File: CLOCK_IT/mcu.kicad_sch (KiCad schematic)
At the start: 25 parts, among them IC1 APS6404L-3SQR-SN, U1 ESP32-S3R8, U2 W25Q128JVSIQ

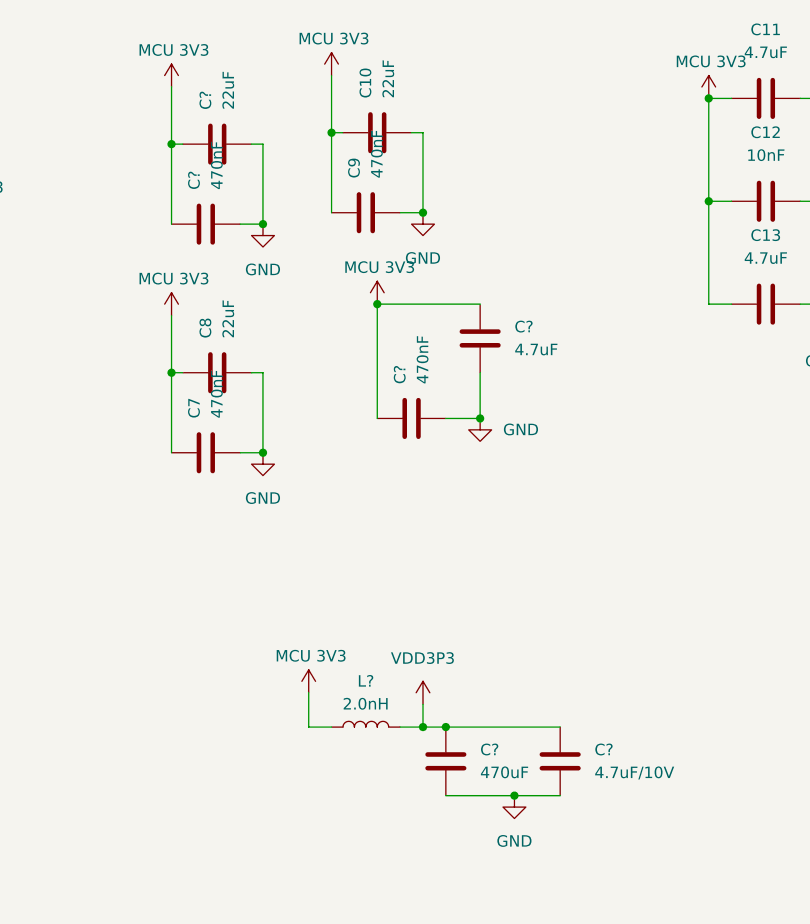
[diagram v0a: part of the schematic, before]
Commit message: :style: renaming capaciors, checking for errors
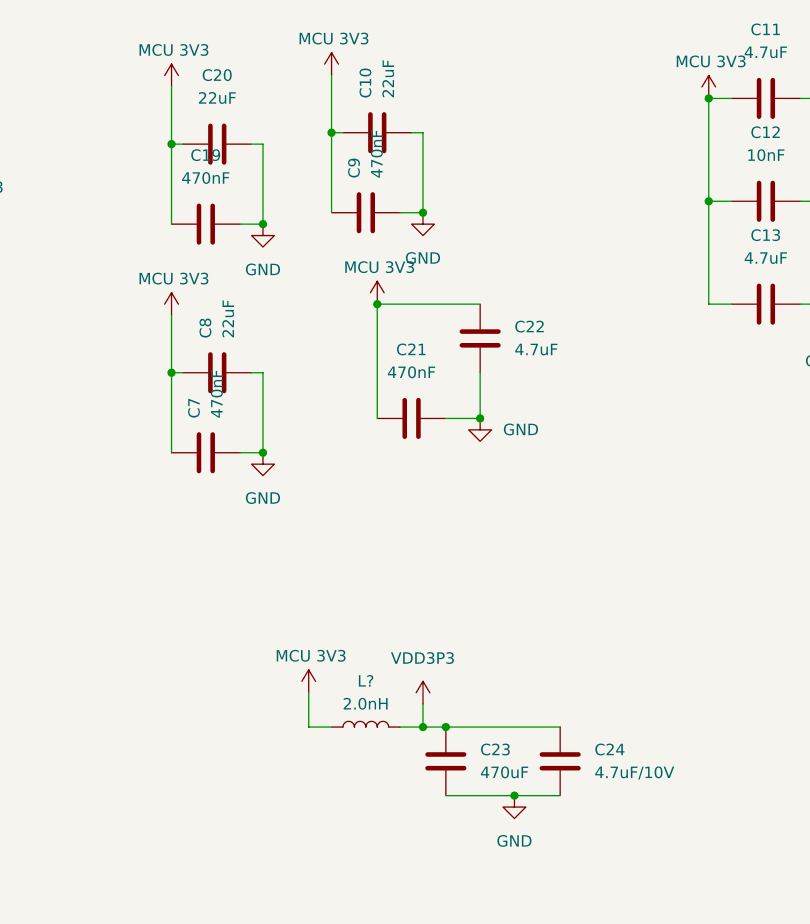
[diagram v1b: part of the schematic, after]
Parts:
- gave numbers to parts that had none: 6
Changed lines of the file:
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@@
 		(dnp no)
 		(fields_autoplaced yes)
-		(property "Reference" "C?"
+		(property "Reference" "C23"
 			(at 233.68 93.9799 0)
 			(effects
@@
 			(project "CLOCK_IT"
 				(path "/6c8f4e2a-0be1-4eb1-92e1-07339040f4c9/25a0942f-4692-4437-8e26-71d966c353a5"
-					(reference "C?")
+					(reference "C23")
 					(unit 1)
 				)
@@
 		(dnp no)
 		(fields_autoplaced yes)
-		(property "Reference" "C?"
-			(at 224.7899 53.34 0)
-			(effects
-				(font
-					(size 1.27 1.27)
-				)
-				(justify left)
+		(property "Reference" "C21"
+			(at 226.06 49.53 90)
+			(effects
+				(font
+					(size 1.27 1.27)
+				)
 			)
 		)
 		(property "Value" "470nF"
-			(at 227.3299 53.34 0)
-			(effects
-				(font
-					(size 1.27 1.27)
-				)
-				(justify left)
+			(at 226.06 52.07 90)
+			(effects
+				(font
+					(size 1.27 1.27)
+				)
 			)
 		)
@@
 			(project "CLOCK_IT"
 				(path "/6c8f4e2a-0be1-4eb1-92e1-07339040f4c9/25a0942f-4692-4437-8e26-71d966c353a5"
-					(reference "C?")
+					(reference "C21")
 					(unit 1)
 				)
@@
 		(dnp no)
 		(fields_autoplaced yes)
-		(property "Reference" "C?"
-			(at 201.9299 31.75 0)
-			(effects
-				(font
-					(size 1.27 1.27)
-				)
-				(justify left)
+		(property "Reference" "C19"
+			(at 203.2 27.94 90)
+			(effects
+				(font
+					(size 1.27 1.27)
+				)
 			)
 		)
 		(property "Value" "470nF"
-			(at 204.4699 31.75 0)
-			(effects
-				(font
-					(size 1.27 1.27)
-				)
-				(justify left)
+			(at 203.2 30.48 90)
+			(effects
+				(font
+					(size 1.27 1.27)
+				)
 			)
 		)
@@
 			(project "CLOCK_IT"
 				(path "/6c8f4e2a-0be1-4eb1-92e1-07339040f4c9/25a0942f-4692-4437-8e26-71d966c353a5"
-					(reference "C?")
+					(reference "C19")
 					(unit 1)
 				)
@@
 		(dnp no)
 		(fields_autoplaced yes)
-		(property "Reference" "C?"
+		(property "Reference" "C24"
 			(at 246.38 93.9799 0)
 			(effects
@@
 			(project "CLOCK_IT"
 				(path "/6c8f4e2a-0be1-4eb1-92e1-07339040f4c9/25a0942f-4692-4437-8e26-71d966c353a5"
-					(reference "C?")
+					(reference "C24")
 					(unit 1)
 				)
@@
 		(dnp no)
 		(fields_autoplaced yes)
-		(property "Reference" "C?"
-			(at 203.1999 22.86 0)
-			(effects
-				(font
-					(size 1.27 1.27)
-				)
-				(justify left)
+		(property "Reference" "C20"
+			(at 204.47 19.05 90)
+			(effects
+				(font
+					(size 1.27 1.27)
+				)
 			)
 		)
 		(property "Value" "22uF"
-			(at 205.7399 22.86 0)
-			(effects
-				(font
-					(size 1.27 1.27)
-				)
-				(justify left)
+			(at 204.47 21.59 90)
+			(effects
+				(font
+					(size 1.27 1.27)
+				)
 			)
 		)
@@
 			(project "CLOCK_IT"
 				(path "/6c8f4e2a-0be1-4eb1-92e1-07339040f4c9/25a0942f-4692-4437-8e26-71d966c353a5"
-					(reference "C?")
+					(reference "C20")
 					(unit 1)
 				)
@@
 		(dnp no)
 		(fields_autoplaced yes)
-		(property "Reference" "C?"
+		(property "Reference" "C22"
 			(at 237.49 46.9899 0)
 			(effects
@@
 			(project "CLOCK_IT"
 				(path "/6c8f4e2a-0be1-4eb1-92e1-07339040f4c9/25a0942f-4692-4437-8e26-71d966c353a5"
-					(reference "C?")
-					(unit 1)
-				)
+					(reference "C22")
+					(unit 1)
+				)

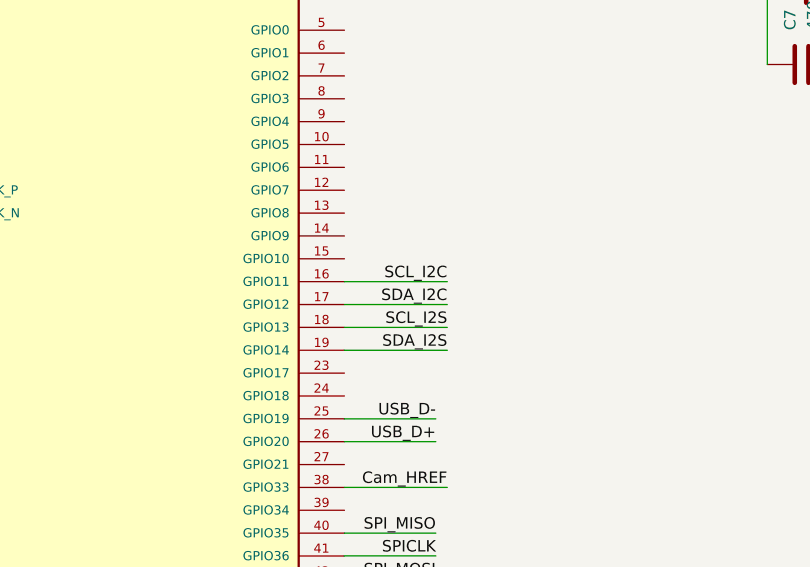
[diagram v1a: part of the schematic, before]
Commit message: :fire: adding I2C communication
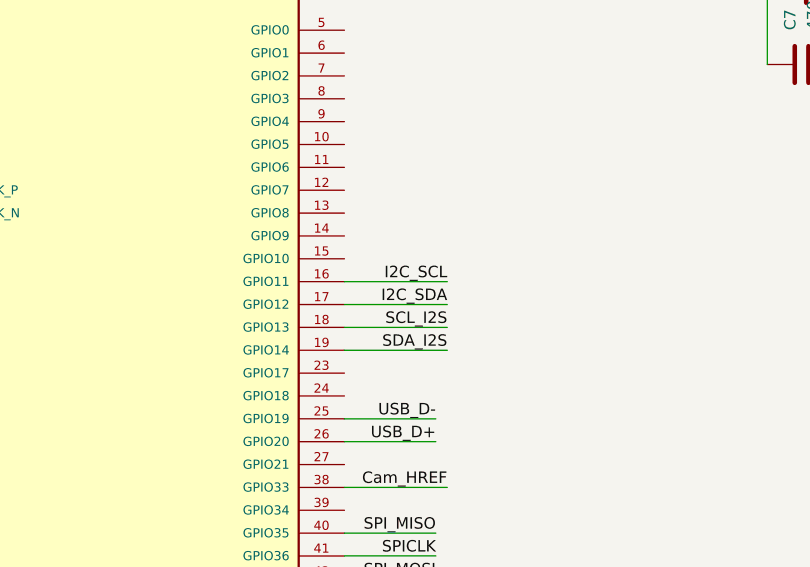
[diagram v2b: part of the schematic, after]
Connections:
- net SCL_I2C renamed I2C_SCL
- net SDA_I2C renamed I2C_SDA
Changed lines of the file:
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@@
-		)
-	)
-	(label "SCL_I2C"
-		(at 163.83 85.09 180)
-		(effects
-			(font
-				(size 1.27 1.27)
-			)
-			(justify right bottom)
 		)
 	)
@@
 		)
 	)
-	(label "SDA_I2C"
-		(at 163.83 87.63 180)
-		(effects
-			(font
-				(size 1.27 1.27)
-			)
-			(justify right bottom)
-		)
-	)
 	(label "Flash WP"
 		(at 90.17 113.03 0)
@@
 			)
 			(justify left bottom)
+		)
+	)
+	(label "I2C_SCL"
+		(at 163.83 85.09 180)
+		(effects
+			(font
+				(size 1.27 1.27)
+			)
+			(justify right bottom)
 		)
 	)
@@
 		(effects
 			(font
+				(size 1.27 1.27)
+			)
+			(justify right bottom)
+		)
+	)
+	(label "I2C_SDA"
+		(at 163.83 87.63 180)
+		(effects
+			(font
